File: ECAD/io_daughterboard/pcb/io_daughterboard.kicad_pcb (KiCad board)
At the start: 2 copper layers, 120 x 66 mm, 90 parts, among them CON1 BARREL_JACK, J1 XF2L-0625-1A, J2 FH12A-40S-0.5SH, P1 CONN_02X32, P10 Slave 5B, P11 Slave 1C, P12 Slave 3C, P13 Slave 4C, P14 Slave 5C, P15 Slave 1D, P16 Slave 3D, P17 Slave 4D, P18 Slave 5D, P19 MIDI, P2 CONN_02X32, P3 Slave 1A, P4 Slave 3A, P5 Slave 4A, P6 Slave 5A, P7 Slave 1B, P8 Slave 3B, P9 Slave 4B, SW1 Reset, SW2 User, U1 FAN5333BSX, U10 SN74LV1T34DCKR, U11 SN74LV1T34DCKR, U2 SPX3819M5-L-3-3, U3 74HC244, U4 74HC244, U5 74HC244, U6 STMPE811QTR, U7 74HC244, U8 74HC244, U9 74HC244

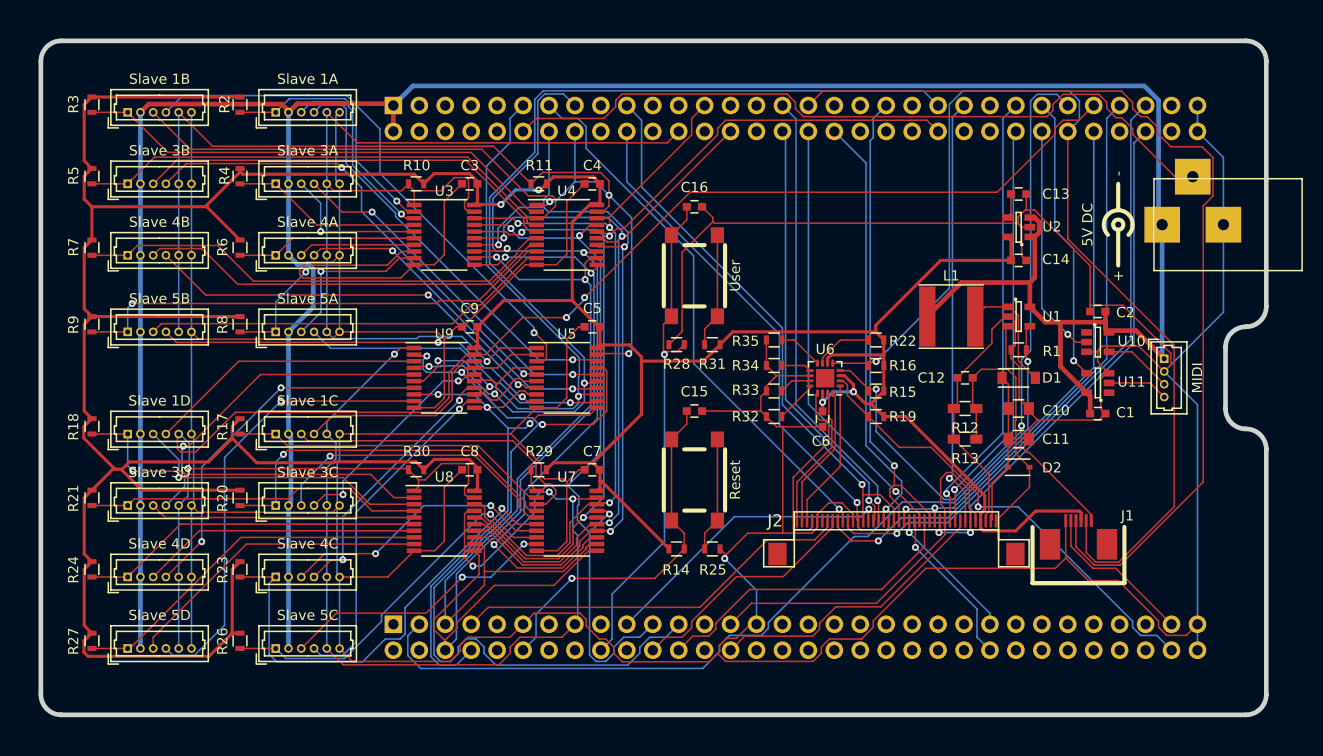
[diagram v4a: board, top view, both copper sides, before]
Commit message: Added copper pours front and back for ground.
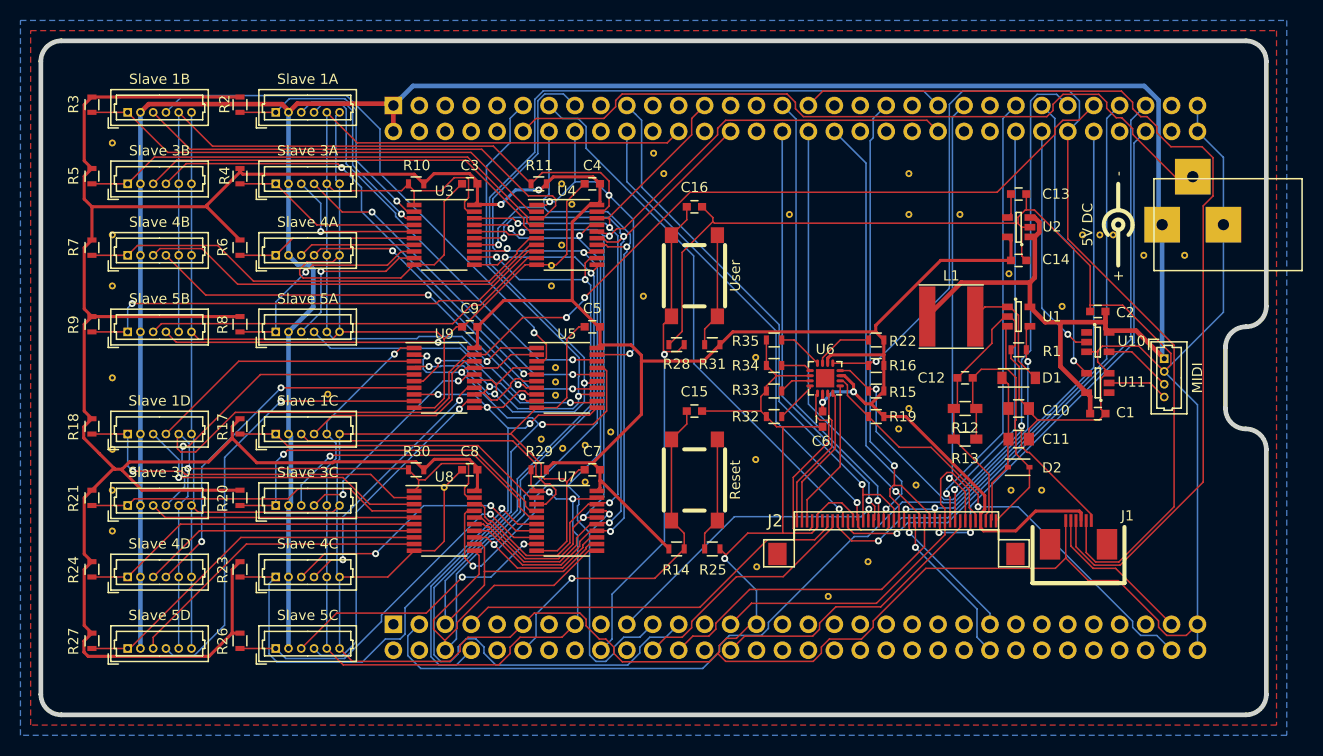
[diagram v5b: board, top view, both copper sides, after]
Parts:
- added REF**: Via, Via, F.Cu at (107.0, 78.0)
- added REF**: Via, Via, F.Cu at (160.0, 45.0)
- added REF**: Via, Via, F.Cu at (159.0, 59.0)
- added REF**: Via, Via, F.Cu at (184.0, 72.0)
- added REF**: Via, Via, F.Cu at (195.0, 78.0)
- added REF**: Via, Via, F.Cu at (198.0, 78.0)
- added REF**: Via, Via, F.Cu at (170.1, 85.5)
- added REF**: Via, Via, F.Cu at (181.0, 85.0)
- added REF**: Via, Via, F.Cu at (185.0, 47.0)
- added REF**: Via, Via, F.Cu at (128.1, 68.6)
- added REF**: Via, Via, F.Cu at (150.4, 66.0)
- added REF**: Via, Via, F.Cu at (107.0, 82.0)
- added REF**: Via, Via, F.Cu at (150.4, 67.4)
- added REF**: Via, Via, F.Cu at (150.4, 68.7)
- added REF**: Via, Via, F.Cu at (151.1, 73.9)
- added REF**: Via, Via, F.Cu at (153.3, 77.2)
- added REF**: Via, Via, F.Cu at (155.8, 72.3)
- added REF**: Via, Via, F.Cu at (153.3, 73.6)
- added REF**: Via, Via, F.Cu at (149.0, 73.0)
- added REF**: Via, Via, F.Cu at (151.0, 54.0)
- added REF**: Via, Via, F.Cu at (151.0, 48.0)
- added REF**: Via, Via, F.Cu at (152.0, 50.0)
- added REF**: Via, Via, F.Cu at (107.0, 74.0)
- added REF**: Via, Via, F.Cu at (150.0, 56.0)
- added REF**: Via, Via, F.Cu at (150.0, 58.0)
- added REF**: Via, Via, F.Cu at (203.7, 53.0)
- added REF**: Via, Via, F.Cu at (194.8, 56.8)
- added REF**: Via, Via, F.Cu at (185.7, 77.5)
- added REF**: Via, Via, F.Cu at (173.3, 51.0)
- added REF**: Via, Via, F.Cu at (212.0, 55.0)
- added REF**: Via, Via, F.Cu at (208.0, 55.0)
- added REF**: Via, Via, F.Cu at (205.0, 53.0)
- added REF**: Via, Via, F.Cu at (202.0, 53.0)
- added REF**: Via, Via, F.Cu at (107.0, 44.0)
- added REF**: Via, Via, F.Cu at (139.5, 77.7)
- added REF**: Via, Via, F.Cu at (170.0, 65.0)
- added REF**: Via, Via, F.Cu at (170.0, 75.0)
- added REF**: Via, Via, F.Cu at (200.0, 60.0)
- added REF**: Via, Via, F.Cu at (185.0, 70.0)
- added REF**: Via, Via, F.Cu at (190.0, 51.0)
- added REF**: Via, Via, F.Cu at (185.0, 51.0)
- added REF**: Via, Via, F.Cu at (107.0, 53.0)
- added REF**: Via, Via, F.Cu at (107.0, 58.0)
- added REF**: Via, Via, F.Cu at (107.0, 67.0)
- added REF**: Via, Via, F.Cu at (177.1, 88.4)
- added REF**: Via, Via, F.Cu at (161.0, 47.0)
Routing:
- added copper zone on B.Cu, net GND
- added copper zone on F.Cu, net GND
